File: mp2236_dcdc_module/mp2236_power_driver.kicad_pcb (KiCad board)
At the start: 2 copper layers, 30 x 20 mm, 21 parts, among them J1 VIN, J2 GND, J3 VOUT, J4 GND, U1 MP2236CGJ-Z

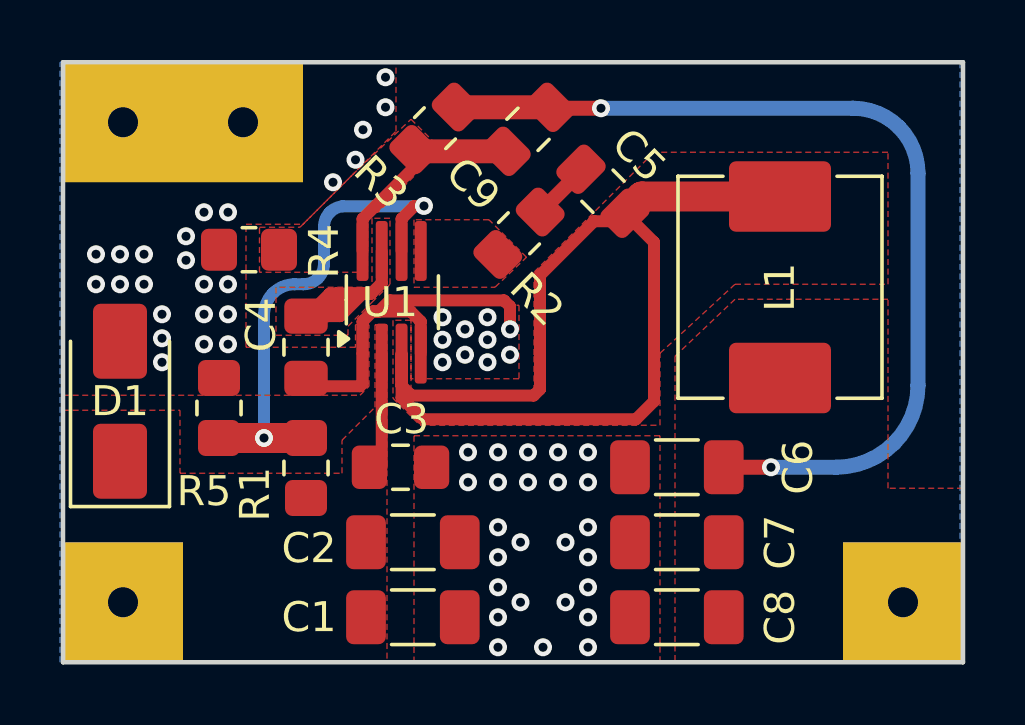
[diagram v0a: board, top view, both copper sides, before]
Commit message: mp2236 power module v1.1
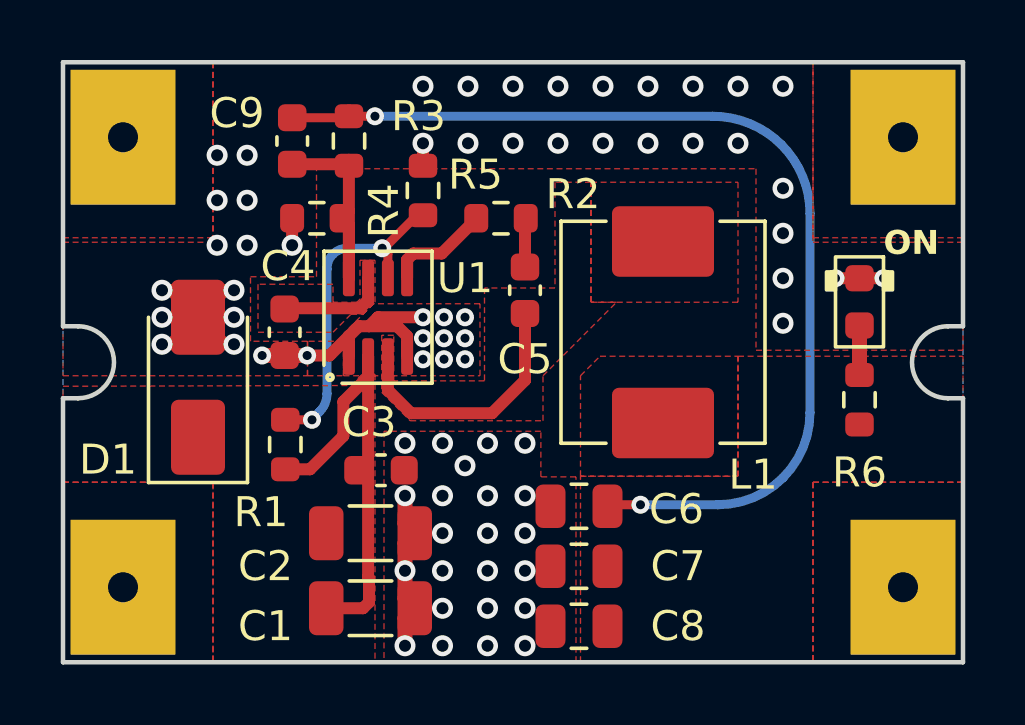
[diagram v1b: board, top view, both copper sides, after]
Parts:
- removed J3: VOUT, power_driver:3mmx3mm power pad
- removed J4: GND, power_driver:3mmx3mm power pad
- added LED1: LED_0603_Green, PCM_LED_SMD_AKL:LED_0603_1608Metric, F.Cu at (136.6, 68.0)
- added R6: 5.1K, Resistor_SMD:R_0603_1608Metric, F.Cu at (136.6, 71.2)
- C1, C2: footprint Capacitor_SMD:C_1206_3216Metric_Pad1.33x1.80mm_HandSolder -> Capacitor_SMD:C_1206_3216Metric
- C3, C4, C5, C9: footprint Capacitor_SMD:C_0805_2012Metric_Pad1.18x1.45mm_HandSolder -> Capacitor_SMD:C_0603_1608Metric
- C6, C7, C8: footprint Capacitor_SMD:C_1206_3216Metric_Pad1.33x1.80mm_HandSolder -> Capacitor_SMD:C_0805_2012Metric
- J1: value VIN -> Conn_01x02_Socket; footprint power_driver:3mmx3mm power pad -> power_driver:4mmx5mm_2x18.0mm power pad
- J2: value GND -> Conn_01x02_Socket; footprint power_driver:3mmx3mm power pad -> power_driver:4mmx5mm_2x18.0mm power pad
- R1, R2, R3, R4, R5: footprint Resistor_SMD:R_0805_2012Metric_Pad1.20x1.40mm_HandSolder -> Resistor_SMD:R_0603_1608Metric
- U1: footprint Package_TO_SOT_SMD:TSOT-23-8_HandSoldering -> PCM_Package_TO_SOT_SMD_AKL:TSOT-23-8
- moved J2 23.4 mm to (138.0, 70.0), turned to 90 degrees
- moved R5 9.94 mm to (122.0, 64.3)
- moved J1 8.00 mm to (112.0, 70.0), turned to 90 degrees
- moved C9 7.87 mm to (117.6, 62.6), turned to -90 degrees
- moved C5 4.20 mm to (125.4, 67.6), turned to -90 degrees
- moved L1 4.18 mm to (130.0, 69.0)
- moved C6 3.51 mm to (127.2, 74.8)
- moved C7 3.36 mm to (127.2, 76.8)
- moved C8 3.28 mm to (127.2, 78.8)
- moved R3 2.90 mm to (119.5, 62.6), turned to -90 degrees
- moved D1 2.72 mm to (114.5, 70.5)
- moved R4 2.49 mm to (118.5, 65.2)
- moved C1 1.44 mm to (120.2, 78.2)
- moved C2 1.44 mm to (120.2, 75.7)
- moved R1 1.04 mm to (117.4, 72.7)
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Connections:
- J2 pad 1: GND -> +5V
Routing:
- net /SW: track 35.9 -> 8.69 mm
- net +12V: track 3.79 -> 15.4 mm
- net GND: track 13.8 -> 23.7 mm, vias 59 -> 70
- net /VCC: track 10.1 -> 3.93 mm
- net Net-(U1-EN): track 16.8 -> 11.2 mm
- net /BST: track 0.00 -> 3.50 mm
- net +5V: track 31.8 -> 34.0 mm
- net Net-(LED1-A): track 0.00 -> 1.65 mm
- net /FB: track 7.28 -> 8.29 mm
- net Net-(C5-Pad1): track 2.21 -> 1.64 mm
- removed copper zone on F.Cu, net /BST
- removed copper zone on F.Cu, net /FB
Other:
- outline, holes or cut-outs redrawn
- board text added: "MP2236 DCDC MODULE VERSION: 1.1 DATE: 2024-12-22"
- board text added: "ON"
- board text removed: "MP2236 DCDC MODULE VERSION: 1.0 DATE: 2024-12-11"
